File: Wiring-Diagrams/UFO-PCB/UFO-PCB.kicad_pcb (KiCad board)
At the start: 2 copper layers, 10 parts, among them M1 Motor_Servo, M2 Motor_Servo, M3 Motor_Servo, M4 Motor_Servo, U1 NRF24L01_Breakout

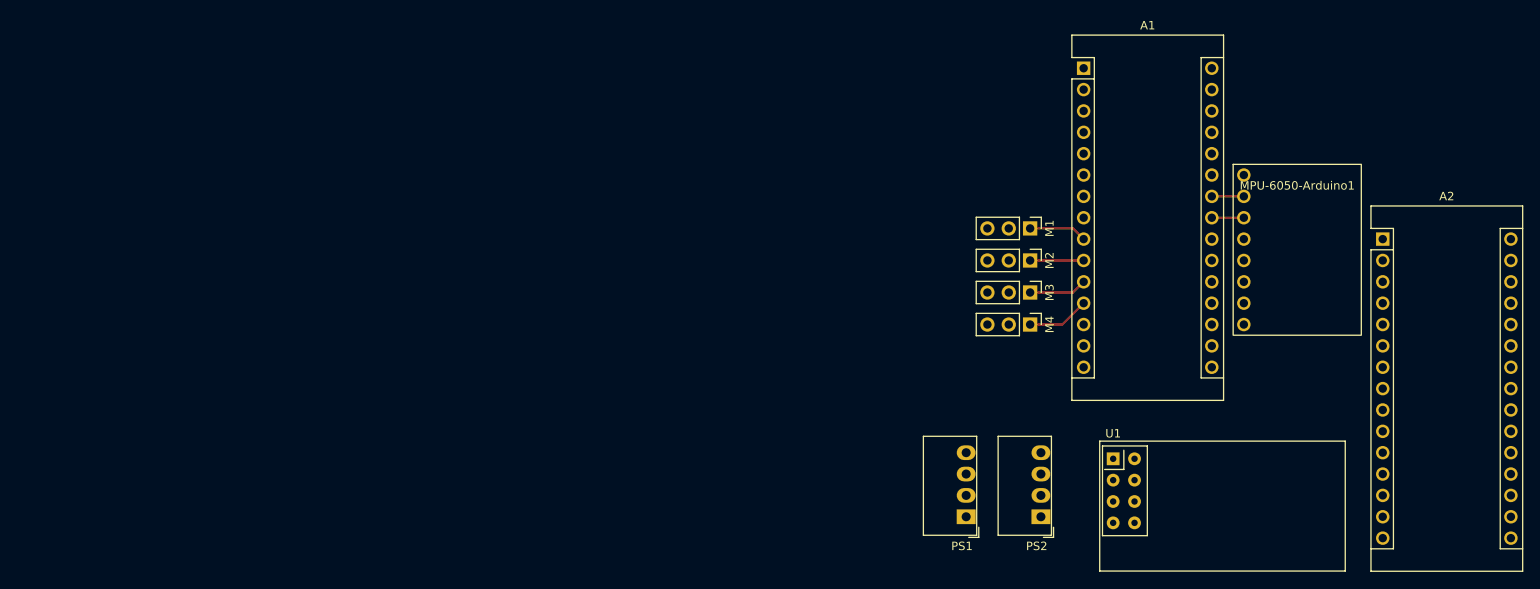
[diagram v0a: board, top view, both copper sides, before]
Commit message: Update Controller PCB with all components, no traces yet
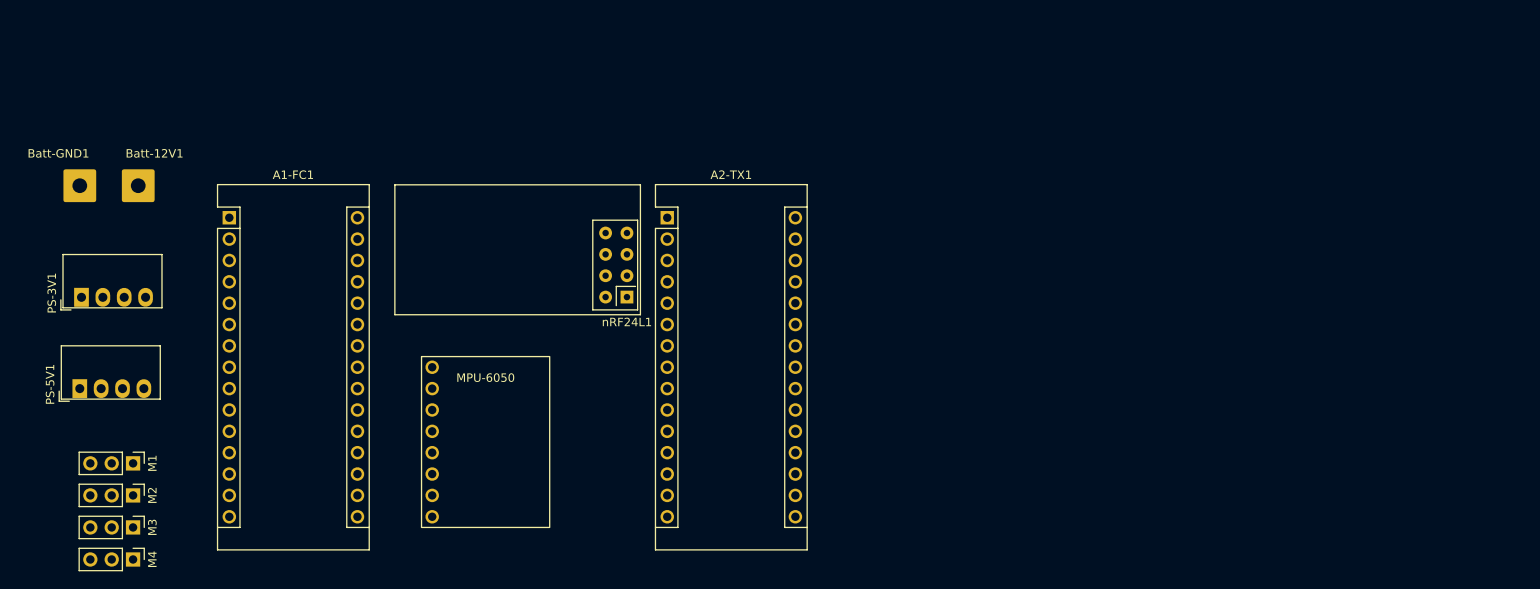
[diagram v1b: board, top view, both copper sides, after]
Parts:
- removed A1, A2: Arduino_Nano_v3.x, Module:Arduino_Nano
- removed MPU-6050-Arduino1: MPU-6050-Arduino, Sensor_Motion:MPU-6050-Arduino
- removed PS1, PS2: MEE1S0305SC, Converter_DCDC:Converter_DCDC_Murata_MEE1SxxxxSC_THT
- removed U1: NRF24L01_Breakout, RF_Module:nRF24L01_Breakout
- added A1-FC1: Arduino_Nano_v3.x, Module:Arduino_Nano, F.Cu at (53.3, 62.2)
- added A2-TX1: Arduino_Nano_v3.x, Module:Arduino_Nano, F.Cu at (105.4, 62.2)
- added Batt-12V1: Conn_01x01_Male, Connector_Wire:SolderWire-1sqmm_1x01_D1.4mm_OD3.9mm, F.Cu at (42.5, 58.4)
- added Batt-GND1: Conn_01x01_Male, Connector_Wire:SolderWire-1sqmm_1x01_D1.4mm_OD3.9mm, F.Cu at (35.6, 58.4)
- added MPU-6050: MPU-6050-Breakout, Sensor_Motion:MPU-6050-Breakout, F.Cu at (83.8, 88.9)
- added PS-3V1: MEE1S0305SC, Converter_DCDC:Converter_DCDC_Murata_MEE1SxxxxSC_THT, F.Cu at (35.8, 71.7)
- added PS-5V1: MEE1S0305SC, Converter_DCDC:Converter_DCDC_Murata_MEE1SxxxxSC_THT, F.Cu at (35.6, 82.5)
- added nRF24L1: NRF24L01_Breakout, RF_Module:nRF24L01_Breakout, F.Cu at (100.6, 71.7)
- moved M1 110.3 mm to (41.9, 91.4)
- moved M2 110.3 mm to (41.9, 95.2)
- moved M3 110.3 mm to (41.9, 99.1)
- moved M4 110.3 mm to (41.9, 102.9)
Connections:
- M1 pad 2: Net-(A1-Pad30) -> Net-(A1-FC1-Pad4)
- M1 pad 3: Net-(A1-Pad4) -> Net-(A1-FC1-Pad4)
- M2 pad 2: Net-(A1-Pad30) -> Net-(A1-FC1-Pad4)
- M2 pad 3: Net-(A1-Pad4) -> Net-(A1-FC1-Pad4)
- M3 pad 2: Net-(A1-Pad30) -> Net-(A1-FC1-Pad4)
- M3 pad 3: Net-(A1-Pad4) -> Net-(A1-FC1-Pad4)
- M4 pad 2: Net-(A1-Pad30) -> Net-(A1-FC1-Pad4)
- M4 pad 3: Net-(A1-Pad4) -> Net-(A1-FC1-Pad4)
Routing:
- net Net-(A1-FC1-Pad12): track 7.42 -> 0.00 mm
- net Net-(A1-FC1-Pad11): track 6.89 -> 0.00 mm
- net Net-(A1-FC1-Pad9): track 6.89 -> 0.00 mm
- net Net-(A1-FC1-Pad10): track 6.37 -> 0.00 mm
- net Net-(A1-Pad24): track 3.81 -> 0.00 mm
- net Net-(A1-Pad23): track 3.81 -> 0.00 mm
